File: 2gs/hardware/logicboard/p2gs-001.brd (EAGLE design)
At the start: 91 x 90 mm, 66 parts, among them J1 MKR, J10 1-Wire, J2 GPIO, J3 Vcc, J5 SPI, J6 LED, J7 DIN5, K1 G5V1, Q1 220mA/50V/3.5Ω, Q2 220mA/50V/3.5Ω, T1 2SC1815

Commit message: Routed.
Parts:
- removed A, B: (no value), wirepad:SMD1,27-2,54
- removed C1: 22u, rcl:C025-050X050
- removed C10, C11, C4: 100n, rcl:C025-024X044
- removed C12, C13, C3: 1u, rcl:C050-024X044
- removed C2: 470n, rcl:C050-024X044
- removed C5: 10n, resistor:C025-024X044
- removed DISP1: AQM0802A-RN-GBW, AQM0802A-RN-GBW:AQM0802A-RN-GBW-FOOTPRINT
- removed DISP2: MNTR, pinhead:1X04
- removed F1: 1.8A, fuse:TE5
- removed H1, H2: STAND-OFF, SparkFun-Hardware:STAND-OFF
- removed J10: 1-Wire, SparkFun-Connectors:JST-3-PTH-VERT
- removed J20: (no value), SparkFun-Connectors:1X04_1.27MM
- removed J3: Vcc, SparkFun-Connectors:JST-2-PTH
- removed J5: SPI, SparkFun-Connectors:1X06_1.27MM
- removed J6: LED, SparkFun-Connectors:JST-3-PTH-VERT
- removed JP1: PWRSEL, pinhead:2X03
- removed JP2: RTC, SparkFun-Connectors:1X05
- removed JP4: RLYJMP, pinhead:1X02
- removed JP5: PWR, pinhead:1X03
- removed JP6: LED, pinhead:1X03
- removed K1: G5V1, relay:G5V1
- removed R1, R3: 1k, resistor:0204/5
- removed R101, R102, R103, R104: 10k, rcl:M2012
- removed R2: 47k, resistor:0204/5
- removed RN2: 4.7k, resistor-net:RN-5
- removed RN4: 220, resistor-dil:DIL16
- removed RZ1***, RZ2***, RZ3**, RZ4**, VCCBRIDGE***: Inf, rcl:M2012
- removed T1: 2SC1815, transistor:TO92-ECB
- removed V1: 5V, v-reg:78XXL
- removed VDDBRIDGE: 0, rcl:M2012
- added D10, D11, D12, D13, D14, D15, D16, D4, D5, D6, D7, D8, D9: 200mA/100V/1V, SparkFun-DiscreteSemi:DIODE-1N4148
- added D20: (no value), SparkFun-DiscreteSemi:DIODE-1N4148
- added LD1: Red/Green, led:DUOLED-C-5MM
- added Q10, Q11, Q12, Q13, Q14, Q15, Q16, Q3, Q4, Q5, Q6, Q7, Q8, Q9: 60V/32A/35mΩ, SparkFun-DiscreteSemi:TO220V
- added R6: 220, resistor:0204/5
- added X1: ADAFRUIT-PCA9685, adafruit-pca9685:ADAFRUIT-PCA9685-FOOTPRINT
- D1, D2, D3: value (none) -> 200mA/100V/1V
- J0: value (none) -> 12V
- J2: value GPIO -> (none); device SparkFun-Connectors:JST-4-PTH -> Connector:4P-2.0-90D
- Q1, Q2: value 220mA/50V/3.5Ω -> 60V/32A/35mΩ; device SparkFun-DiscreteSemi:SOT23-3 -> SparkFun-DiscreteSemi:TO220V
- R4, R5: value 1k -> 330
- SV2: value (none) -> LD
- moved J2 82.1 mm to (73.0, 81.5), turned to 0 degrees
- moved C8 58.8 mm to (29.0, 32.0)
- moved C9 57.8 mm to (29.0, 38.0)
- moved U$1 51.1 mm to (35.0, 76.0)
- moved Q1 36.5 mm to (51.5, 50.0), flipped to the top, turned to 0 degrees
- moved D2 35.0 mm to (62.5, 55.0), turned to 0 degrees
- moved C7 32.9 mm to (80.5, 69.0)
- moved D1 30.6 mm to (51.5, 55.0), turned to 0 degrees
- moved C6 29.5 mm to (69.0, 64.0)
- moved OK1 29.5 mm to (62.0, 64.0)
- moved RN3 28.9 mm to (49.0, 64.0), turned to 270 degrees
- moved D3 28.3 mm to (73.5, 55.0), turned to 0 degrees
- moved R5 26.5 mm to (29.0, 18.0), turned to 90 degrees
- moved Q2 23.6 mm to (62.5, 50.0), flipped to the top, turned to 0 degrees
- moved R4 20.4 mm to (29.0, 26.0), turned to 90 degrees
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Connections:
- removed net CAP1N: C12.2, DISP1.3
- removed net CAP1P: C12.1, DISP1.4
- removed net LCDVOUT: C13.2, DISP1.2
- removed net MNTRA: OK1.4, RN4.16
- removed net NMO2RTN: RN2.5
- removed net NMORTN: RN2.4
- removed net NMTRTN: RN2.3
- removed net RLYDRV: R1.1, R2.2, T1.B
- removed net RLYOUT: K1.10
- removed net RLYOUT1: RZ3**.2
- removed net RLYOUT2: RZ4**.2
- removed net RLYSNK: D2.A, K1.9, T1.C
- removed net SCL3V: DISP1.8, Q1.2, R102.1, RZ1***.2
- removed net SDA3V: DISP1.7, Q2.2, R104.1, RZ2***.2
- removed net V+: C1.1, C2.1, D1.C, J0.3, JP1.1, JP5.3, V1.IN
- removed net VCC/2: JP1.5, R3.2, RN4.1
- removed net VCC/VDD: C11.1, C13.1, DISP1.5, DISP1.9, VCCBRIDGE***.1, VDDBRIDGE.1
- removed net VOUT: F1.2, JP1.4, JP1.6
- removed net VOUTRAW: B.1, C3.1, C4.1, D1.A, J3.2, JP4.2, K1.5, K1.6, RZ3**.1, V1.OUT
- removed net VOUTRAW2: A.1, F1.1, JP4.1, K1.1, RZ4**.1
- new net LD00: D1.A, Q1.2, SV2.1
- new net LD01: D2.A, Q2.2, SV2.3
- new net LD02: D3.A, Q3.2, SV2.5
- new net LD03: D4.A, Q4.2, SV2.7
- new net LD04: D5.A, Q5.2, SV2.9
- new net LD05: D6.A, Q6.2, SV2.11
- new net LD06: D7.A, Q7.2, SV2.13
- new net LD07: D8.A, Q8.2, SV2.15
- new net LD08: D9.A, Q9.2, SV2.17
- new net LD09: D10.A, Q10.2, SV2.19
- new net LD10: D11.A, Q11.2, SV2.21
- new net LD11: D12.A, Q12.2, SV2.23
- new net LD12: D13.A, Q13.2, SV2.25
- new net LD13: D14.A, Q14.2, SV2.27
- new net LD14: D15.A, Q15.2, SV2.29
- new net LD15: D16.A, Q16.2, SV2.31
- new net PWM00: Q1.1, X1.PWM00
- new net PWM01: Q2.1, X1.PWM01
- new net PWM02: Q3.1, X1.PWM02
- new net PWM03: Q4.1, X1.PWM03
- new net PWM04: Q5.1, X1.PWM04
- new net PWM05: Q6.1, X1.PWM05
- new net PWM06: Q7.1, X1.PWM06
- new net PWM07: Q8.1, X1.PWM07
- new net PWM08: Q9.1, X1.PWM08
- new net PWM09: Q10.1, X1.PWM09
- new net PWM10: Q11.1, X1.PWM10
- new net PWM11: Q12.1, X1.PWM11
- new net PWM12: Q13.1, X1.PWM12
- new net PWM13: Q14.1, X1.PWM13
- new net PWM14: Q15.1, X1.PWM14
- new net PWM15: Q16.1, X1.PWM15
- net AREF: no longer C10.1, R3.1
- net GND: now also J2.4, LD1.C, OK1.4, Q1.3, Q10.3, Q11.3, Q12.3, Q13.3, Q14.3, Q15.3, Q16.3, Q2.3, Q3.3, Q4.3, Q5.3, Q6.3, Q7.3, Q8.3, Q9.3, X1.GND00, X1.GND01, X1.GND02, X1.GND03, X1.GND04, X1.GND05, X1.GND06, X1.GND07, X1.GND08, X1.GND09, X1.GND10, X1.GND11, X1.GND12, X1.GND13, X1.GND14, X1.GND15, X1.LGND, X1.LOE, X1.RGND; no longer C1.2, C10.2, C11.2, C2.2, C3.2, C4.2, C5.2, DISP1.6, DISP2.1, J10.1, J2.1, J3.1, J5.6, J6.2, JP2.2, JP5.1, JP6.2, R2.1, T1.E, V1.GND
- net GPIO0: no longer J2.3, J20.3
- net GPIO1: no longer J2.4, J20.4
- net LED0A: now also LD1.AR; no longer J6.3, JP6.3
- net LED1A: now also LD1.AX; no longer J6.1, JP6.1
- net MIDIINSND: now also D20.C, R6.1; no longer D3.C, RN4.2
- net MIRTN: now also D20.A; no longer D3.A
- net MISND: now also R6.2; no longer RN4.15
- net MISO: no longer J5.1
- net MNTR: no longer OK1.6, RN3.5
- net MOSI: no longer J5.4
- net RLY: no longer R1.2
- net RST: no longer J5.5
- net RX: now also RN3.5; no longer RN2.2
- net SCK: no longer J5.3
- net SCL: now also J2.1, X1.LSCL; no longer DISP2.3, JP2.4, Q1.3, R101.1, RZ1***.1
- net SDA: now also J2.2, X1.LSDA; no longer DISP2.4, JP2.5, Q2.3, R103.1, RZ2***.1
- net THS: no longer J10.2, RN3.4
- net VCC: now also J2.3, X1.LVCC; no longer C5.1, D2.C, DISP2.2, J10.3, J2.2, J5.2, JP1.3, JP2.1, JP5.2, K1.2, R101.2, R103.2, RN2.1, VCCBRIDGE***.2
- net VDD: no longer Q1.1, Q2.1, R102.2, R104.2, VDDBRIDGE.2
- net VIN: now also D1.C, D10.C, D11.C, D12.C, D13.C, D14.C, D15.C, D16.C, D2.C, D3.C, D4.C, D5.C, D6.C, D7.C, D8.C, D9.C, J0.3, SV2.10, SV2.12, SV2.14, SV2.16, SV2.18, SV2.2, SV2.20, SV2.22, SV2.24, SV2.26, SV2.28, SV2.30, SV2.32, SV2.4, SV2.6, SV2.8, X1.LV+, X1.RV+, X1.V+00, X1.V+01, X1.V+02, X1.V+03, X1.V+04, X1.V+05, X1.V+06, X1.V+07, X1.V+08, X1.V+09, X1.V+10, X1.V+11, X1.V+12, X1.V+13, X1.V+14, X1.V+15; no longer JP1.2
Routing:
- net GND: track 0.00 -> 448.4 mm, vias 0 -> 1
- net VIN: track 0.00 -> 369.6 mm, vias 0 -> 2
- net VCC: track 0.00 -> 179.8 mm, vias 0 -> 3
- net SCL: track 0.00 -> 173.3 mm, vias 0 -> 2
- net SDA: track 0.00 -> 168.2 mm
- net PWM07: track 0.00 -> 128.0 mm, vias 0 -> 2
- net PWM03: track 0.00 -> 106.5 mm
- net PWM10: track 0.00 -> 104.7 mm, vias 0 -> 2
- net PWM15: track 0.00 -> 98.3 mm, vias 0 -> 2
- net PWM11: track 0.00 -> 97.6 mm, vias 0 -> 4
- net D7GATE: track 0.00 -> 96.8 mm, vias 0 -> 2
- net PWM02: track 0.00 -> 95.0 mm, vias 0 -> 2
- net LD11: track 0.00 -> 81.2 mm
- net PWM14: track 0.00 -> 80.5 mm, vias 0 -> 2
- net DTCT2: track 0.00 -> 76.9 mm
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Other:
- board text removed: "00"
- board text removed: "01"
- board text removed: "02"
- board text removed: "03"
- board text removed: "102"
- board text removed: "12V"
- board text removed: "1u"
- board text removed: "2-472"
- board text removed: "2-M2.5"
- board text removed: "221"
- board text removed: "22u"
- board text removed: "4"
- board text removed: "470n"
- board text removed: "473"
- board text removed: "5"
- board text removed: "5V"
- board text removed: "9"
- board text removed: "AREF"
- board text removed: "Adafruit SSD1306"
- board text removed: "Akizuki AQM0802A-RN-GBW"
- board text removed: "Arduino Only"
- board text removed: "C"
- board text removed: "DISP"
- board text removed: "DS18B20+"
- board text removed: "Direct 5V"
- board text removed: "Do not forget installing RN2 to use MIDI"
- board text removed: "Dual Regulator"
- board text removed: "G0"
- board text removed: "G1"
- board text removed: "G5V-1"
- board text removed: "I"
- board text removed: "I/O"
- board text removed: "I2C"
- board text removed: "L0"
- board text removed: "L1"
- board text removed: "LED"
- board text removed: "LED00"
- board text removed: "LED00 monitors Vcc/2"
- board text removed: "Min. requirement for MIDI IN"
- board text removed: "N"
- board text removed: "NC"
- board text removed: "O"
- board text removed: "O2"
- board text removed: "OUT2"
- board text removed: "PWRSEL"
- board text removed: "REG"
- board text removed: "RST"
- board text removed: "RTC"
- board text removed: "RX"
- board text removed: "SC"
- board text removed: "SD"
- board text removed: "Single Regulator"
- board text removed: "SparkFun Real Time Clock Module (12708)"
- board text removed: "T"
- board text removed: "TH"
- board text removed: "TH*"
- board text removed: "THRU"
- board text removed: "TX"
- board text removed: "TestPort II"
- board text removed: "To use J4**"
- board text removed: "V"

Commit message: Artwork.
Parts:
- moved U$1 46.2 mm to (78.0, 59.0)
- renumbered D20 to D0, J2 to JG1
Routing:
- added copper zone on layer 1, net GND
- added copper zone on layer 16, net GND
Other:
- board text added: "221"
- board text added: "331"
- board text added: "472"
- board text added: "G0"
- board text added: "G1"
- board text added: "Grove"
- board text added: "Pineapple IIgs 0.0.1-X"
- board text added: "RX"
- board text added: "TH"
- board text added: "TX"
- board text added: "Test Port II"
- board text removed: "0.0.1-X"
- board text removed: "2-BSS138"
- board text removed: "3.3V I2C"
- board text removed: "4-103"
- board text removed: "5V I2C***"
- board text removed: "C."
- board text removed: "GPIO"
- board text removed: "I2C/THS*/MNTR"
- board text removed: "IN"
- board text removed: "MIDI"
- board text removed: "MIDI IN"
- board text removed: "MIDI OUT"
- board text removed: "N.C."
- board text removed: "N.O."
- board text removed: "OUT"
- board text removed: "PWR"
- board text removed: "Pineapple IIgs"
- board text removed: "RLY"
- board text removed: "Relay-Common"
- board text removed: "Relay-N.C."
- board text removed: "Relay-N.O."
- board text removed: "SPI"
- board text removed: "THS*"
- board text removed: "V/2"
- board text removed: "Vcc/2"
- board text removed: "Vo"
- board text removed: "Vout"

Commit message: Adding pull-down r.
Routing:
- net GND: track 448.4 -> 0.00 mm, vias 1 -> 0
- net VIN: track 369.6 -> 0.00 mm, vias 2 -> 0
- net VCC: track 179.8 -> 0.00 mm, vias 3 -> 0
- net SCL: track 173.3 -> 0.00 mm, vias 2 -> 0
- net SDA: track 168.2 -> 0.00 mm
- net PWM07: track 128.0 -> 0.00 mm, vias 2 -> 0
- net PWM03: track 106.5 -> 0.00 mm
- net PWM10: track 104.7 -> 0.00 mm, vias 2 -> 0
- net PWM15: track 98.3 -> 0.00 mm, vias 2 -> 0
- net PWM11: track 97.6 -> 0.00 mm, vias 4 -> 0
- net D7GATE: track 96.8 -> 0.00 mm, vias 2 -> 0
- net PWM02: track 95.0 -> 0.00 mm, vias 2 -> 0
- net LD11: track 81.2 -> 0.00 mm
- net PWM14: track 80.5 -> 0.00 mm, vias 2 -> 0
- net DTCT2: track 76.9 -> 0.00 mm
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- removed copper zone on layer 1, net GND
- removed copper zone on layer 16, net GND
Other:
- board text added: "K"
- board text added: "X0"
- board text added: "X1"
- board text added: "X2"
- board text added: "X3"

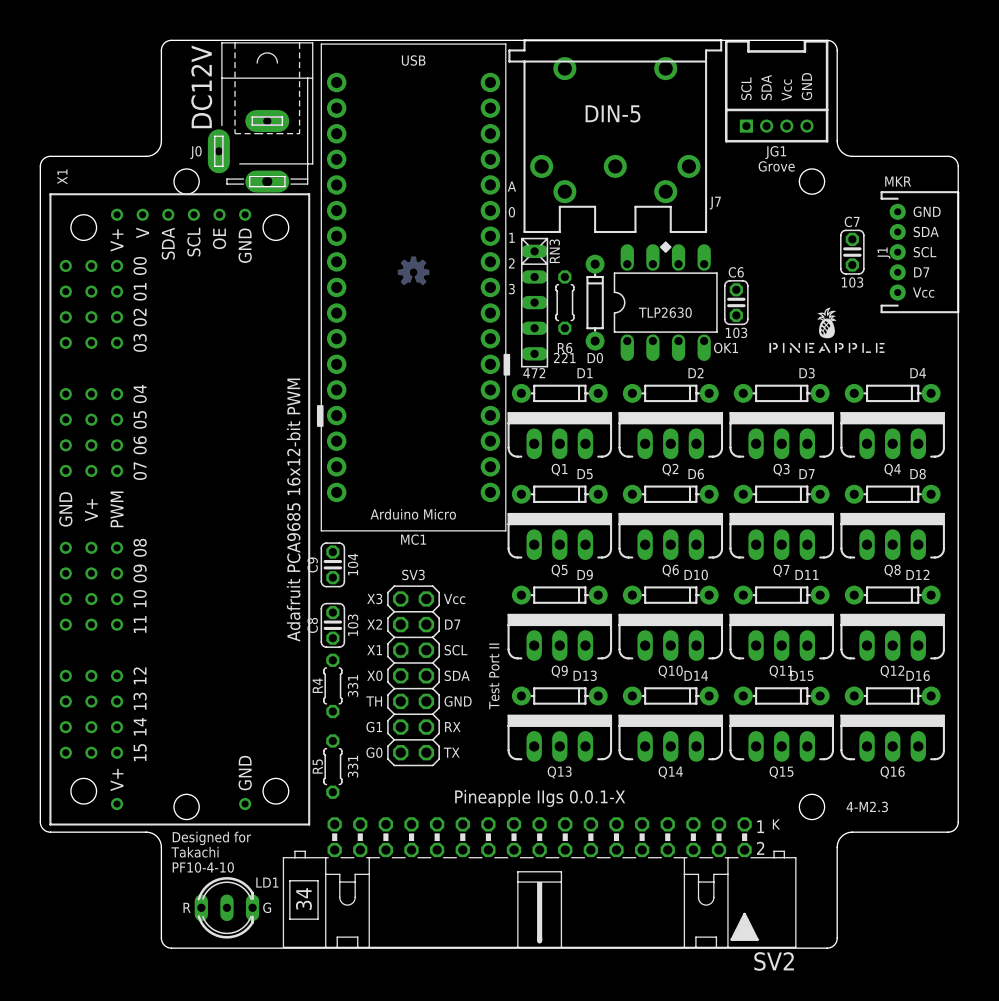
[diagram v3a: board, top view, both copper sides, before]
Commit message: Pull-down.
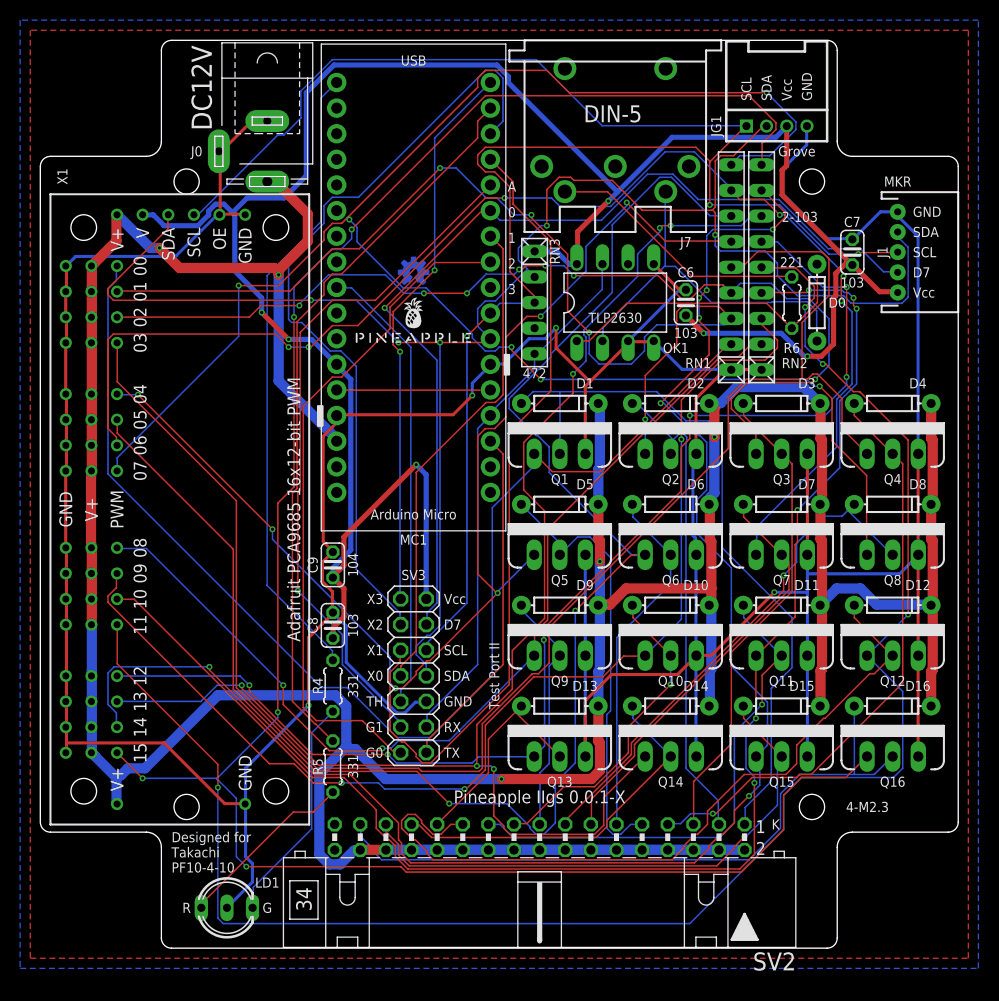
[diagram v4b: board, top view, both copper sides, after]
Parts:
- added RN1, RN2: (no value), resistor-net:RN-9
- moved U$1 41.0 mm to (37.0, 60.0)
- moved R6 22.5 mm to (74.5, 64.0)
- moved D0 22.0 mm to (77.0, 64.0)
- moved C6 5.00 mm to (64.0, 64.0)
- moved OK1 5.00 mm to (57.0, 64.0)
- moved D1 1.00 mm to (51.5, 54.0)
- moved D10 1.00 mm to (62.5, 34.0)
- moved D11 1.00 mm to (73.5, 34.0)
- moved D12 1.00 mm to (84.5, 34.0)
- moved D13 1.00 mm to (51.5, 24.0)
- moved D14 1.00 mm to (62.5, 24.0)
- moved D15 1.00 mm to (73.5, 24.0)
- moved D16 1.00 mm to (84.5, 24.0)
- moved D2 1.00 mm to (62.5, 54.0)
- moved D3 1.00 mm to (73.5, 54.0)
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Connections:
- net GND: now also RN1.1, RN2.1
- net PWM00: now also RN1.2
- net PWM01: now also RN1.3
- net PWM02: now also RN1.4
- net PWM03: now also RN1.5
- net PWM04: now also RN1.6
- net PWM05: now also RN1.7
- net PWM06: now also RN1.8
- net PWM07: now also RN1.9
- net PWM08: now also RN2.2
- net PWM09: now also RN2.3
- net PWM10: now also RN2.4
- net PWM11: now also RN2.5
- net PWM12: now also RN2.6
- net PWM13: now also RN2.7
- net PWM14: now also RN2.8
- net PWM15: now also RN2.9
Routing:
- net GND: track 0.00 -> 456.9 mm, vias 0 -> 4
- net VIN: track 0.00 -> 388.1 mm, vias 0 -> 5
- net VCC: track 0.00 -> 225.4 mm, vias 0 -> 6
- net PWM15: track 0.00 -> 203.3 mm, vias 0 -> 5
- net SCL: track 0.00 -> 178.0 mm, vias 0 -> 3
- net PWM07: track 0.00 -> 173.2 mm, vias 0 -> 6
- net PWM11: track 0.00 -> 171.8 mm, vias 0 -> 4
- net SDA: track 0.00 -> 168.8 mm, vias 0 -> 5
- net PWM14: track 0.00 -> 160.2 mm, vias 0 -> 7
- net PWM05: track 0.00 -> 159.8 mm, vias 0 -> 2
- net PWM03: track 0.00 -> 157.7 mm
- net PWM10: track 0.00 -> 146.3 mm, vias 0 -> 6
- net PWM13: track 0.00 -> 140.3 mm, vias 0 -> 6
- net PWM06: track 0.00 -> 130.8 mm, vias 0 -> 6
- net PWM12: track 0.00 -> 123.1 mm, vias 0 -> 6
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- added copper zone on layer 1, net GND
- added copper zone on layer 16, net GND
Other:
- board text added: "2-103"

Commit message: Double Grove con.
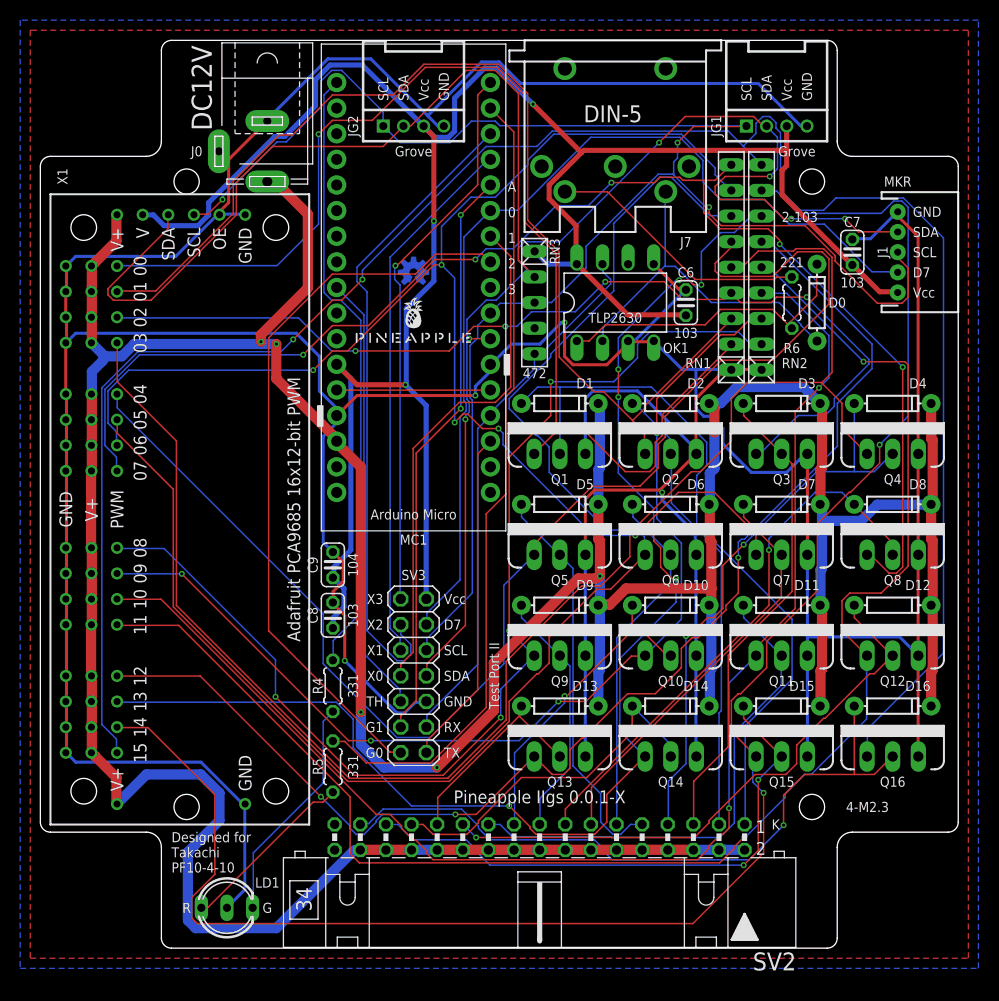
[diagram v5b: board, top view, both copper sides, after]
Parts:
- added JG2: Grove/2, Connector:4P-2.0-90D
- JG1: value (none) -> Grove/1
- RN1, RN2: value (none) -> 10k
- moved C8 1.00 mm to (29.0, 33.0)
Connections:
- net GND: now also JG2.4
- net SCL: now also JG2.1
- net SDA: now also JG2.2
- net VCC: now also JG2.3
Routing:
- net GND: track 456.9 -> 532.2 mm
- net PWM07: track 173.2 -> 134.0 mm, vias 6 -> 5
- net VIN: track 388.1 -> 420.7 mm, vias 5 -> 6
- net DTCT1: track 81.2 -> 53.4 mm
- net SDA: track 168.8 -> 195.9 mm, vias 5 -> 6
- net PWM11: track 171.8 -> 152.9 mm, vias 4 -> 2
- net LD11: track 75.5 -> 58.4 mm, vias 0 -> 1
- net PWM08: track 96.6 -> 113.6 mm, vias 2 -> 4
- net PWM14: track 160.2 -> 174.8 mm, vias 7 -> 2
- net PWM04: track 120.3 -> 134.8 mm, vias 6 -> 0
- net DTCT2: track 78.5 -> 64.4 mm
- net PWM05: track 159.8 -> 146.6 mm, vias 2 -> 0
- net PWM10: track 146.3 -> 134.5 mm, vias 6 -> 2
- net GPIO1: track 68.4 -> 57.4 mm, vias 1 -> 2
- net PWM06: track 130.8 -> 140.9 mm, vias 6 -> 5
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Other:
- board text removed: "USB"
